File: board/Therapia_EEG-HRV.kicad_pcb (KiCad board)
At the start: 4 copper layers, 61.8 x 45 mm, 141 parts, among them J1 USB-C_16P, J2 Header_2x6

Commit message: R29: the 2026-08-29 functional review, applied as BOM-only changes
An independent review found no blocker. Four of its findings can be fixed
without touching a single track, so they are in; the rest are recorded as
Rev.A-accepted, firmware-mandatory, or Rev.B.

  C_CM1P..C_CM8N (16)  C1588  -> C163508   1nF 50V C0G 0603, was X7R
  C_NLDO_OUT           C12530 -> C23733    4.7uF 10V 0402, was 2.2uF 6.3V
  C_LM_IN              C52923 -> C23733    same part, was 1uF 25V
  C_AVDD_P59           C1525  -> C52923    1uF 0402, was 100nF
  C_VCAP1                     kept, with the reason written down

The C0G swap is the one that matters: those sixteen sit on the electrode
input nodes, and X7R is piezoelectric -- in a wearable that is microphonic
noise straight into the ADC -- while its +-10% spread mismatches each
differential pair and caps the 50 Hz CMRR (SBAS499 12.1). JLC has no Basic
C0G in 0603 at all (base-filtered search returns zero), so this adds one
Extended row, 13 -> 14, about $3.07.

The two electrolytic-substitute cases are settled by Samsung's own curves at
25 C rather than by estimate: C12530 holds 0.543 at 2.5 V = 1.19 uF, under
the 2.2 uF TPS72325 asks for (SLVS346 8.2.1.1); C52923 holds 0.420 at 5 V =
0.42 uF against LM2664's 3.3 uF test circuit (SNVS005). C23733's own curve
was not obtained -- flagged in the fixes file and the report. C_VCAP1 stays:
at AVSS+1.1..1.5 V it comes out at 60-65 uF, short of TI's 100 uF but only
in the direction of a shorter start-up wait.

The board diff is 57 property lines on 19 footprints. All 66,242 other lines
of the .kicad_pcb are unchanged, the CPL and the IPC-D-356 are byte-identical,
and all 14 Gerber/drill/job files match the previous export once each file's
one or two generation-date lines are removed. Fields do not plot; this
measures that rather than asserting it. assembly_top.pdf does change -- it
prints Value from F.Fab -- and the 3D previews differ by 0.03% of pixels,
max channel delta 7/255, which is the rayt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
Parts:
- C_AVDD_P59: value 100nF -> 1uF
- C_CM1N, C_CM1P, C_CM2N, C_CM2P, C_CM3N, C_CM3P, C_CM4N, C_CM4P, C_CM5N, C_CM5P, C_CM6N, C_CM6P, C_CM7N, C_CM7P, C_CM8N, C_CM8P: value 1nF -> 1nF 50V C0G 0603
- C_LM_IN: value 1uF -> 4.7uF 10V X5R 0402
- C_NLDO_OUT: value 2.2uF -> 4.7uF 10V X5R 0402
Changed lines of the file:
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@@
 			)
 		)
-		(property "Value" "1nF"
+		(property "Value" "1nF 50V C0G 0603"
 			(at 0 0 0)
 			(layer "F.Fab")
@@
 			)
 		)
-		(property "MPN" "CL10B102KB8NNNC"
+		(property "MPN" "CL10C102JB8NNNC"
 			(at 0 0 0)
 			(layer "Cmts.User")
@@
 			)
 		)
-		(property "LCSC" "C1588"
+		(property "LCSC" "C163508"
 			(at 0 0 0)
 			(layer "Cmts.User")
@@
 			)
 		)
-		(property "Value" "1nF"
+		(property "Value" "1nF 50V C0G 0603"
 			(at 0 0 0)
 			(layer "F.Fab")
@@
 			)
 		)
-		(property "MPN" "CL10B102KB8NNNC"
+		(property "MPN" "CL10C102JB8NNNC"
 			(at 0 0 0)
 			(layer "Cmts.User")
@@
 			)
 		)
-		(property "LCSC" "C1588"
+		(property "LCSC" "C163508"
 			(at 0 0 0)
 			(layer "Cmts.User")
@@
 			)
 		)
-		(property "Value" "1nF"
+		(property "Value" "1nF 50V C0G 0603"
 			(at 0 0 0)
 			(layer "F.Fab")
@@
 			)
 		)
-		(property "MPN" "CL10B102KB8NNNC"
+		(property "MPN" "CL10C102JB8NNNC"
 			(at 0 0 0)
 			(layer "Cmts.User")
@@
 			)
 		)
-		(property "LCSC" "C1588"
+		(property "LCSC" "C163508"
 			(at 0 0 0)
 			(layer "Cmts.User")
@@
 			)
 		)
-		(property "Value" "1nF"
+		(property "Value" "1nF 50V C0G 0603"
 			(at 0 0 0)
 			(layer "F.Fab")
@@
 			)
 		)
-		(property "MPN" "CL10B102KB8NNNC"
+		(property "MPN" "CL10C102JB8NNNC"
 			(at 0 0 0)
 			(layer "Cmts.User")
@@
 			)
 		)
-		(property "LCSC" "C1588"
+		(property "LCSC" "C163508"
 			(at 0 0 0)
 			(layer "Cmts.User")
@@
 			)
 		)
-		(property "Value" "100nF"
+		(property "Value" "1uF"
 			(at 0 0 90)
 			(layer "F.Fab")
@@
 			)
 		)
-		(property "MPN" "CL05B104KO5NNNC"
+		(property "MPN" "CL05A105KA5NQNC"
 			(at 0 0 0)
 			(layer "Cmts.User")
@@
 			)
 		)
-		(property "LCSC" "C1525"
+		(property "LCSC" "C52923"
 			(at 0 0 0)
 			(layer "Cmts.User")
@@
 			)
 		)
-		(property "Value" "1nF"
+		(property "Value" "1nF 50V C0G 0603"
 			(at 0 0 0)
 			(layer "F.Fab")
@@
 			)
 		)
-		(property "MPN" "CL10B102KB8NNNC"
+		(property "MPN" "CL10C102JB8NNNC"
 			(at 0 0 0)
 			(layer "Cmts.User")
@@
 			)
 		)
-		(property "LCSC" "C1588"
+		(property "LCSC" "C163508"
 			(at 0 0 0)
 			(layer "Cmts.User")
@@
 			)
 		)
-		(property "Value" "1nF"
+		(property "Value" "1nF 50V C0G 0603"
 			(at 0 0 0)
 			(layer "F.Fab")
@@
 			)
 		)
-		(property "MPN" "CL10B102KB8NNNC"
+		(property "MPN" "CL10C102JB8NNNC"
 			(at 0 0 0)
 			(layer "Cmts.User")
@@
 			)
 		)
-		(property "LCSC" "C1588"
+		(property "LCSC" "C163508"
 			(at 0 0 0)
 			(layer "Cmts.User")
@@
 			)
 		)
-		(property "Value" "1nF"
+		(property "Value" "1nF 50V C0G 0603"
 			(at 0 0 0)
 			(layer "F.Fab")
@@
 			)
 		)
-		(property "MPN" "CL10B102KB8NNNC"
+		(property "MPN" "CL10C102JB8NNNC"
 			(at 0 0 0)
 			(layer "Cmts.User")
@@
 			)
 		)
-		(property "LCSC" "C1588"
+		(property "LCSC" "C163508"
 			(at 0 0 0)
 			(layer "Cmts.User")
@@
 			)
 		)
-		(property "Value" "1nF"
+		(property "Value" "1nF 50V C0G 0603"
 			(at 0 0 0)
 			(layer "F.Fab")
@@
 			)
 		)
-		(property "MPN" "CL10B102KB8NNNC"
+		(property "MPN" "CL10C102JB8NNNC"
 			(at 0 0 0)
 			(layer "Cmts.User")
@@
 			)
 		)
-		(property "LCSC" "C1588"
+		(property "LCSC" "C163508"
 			(at 0 0 0)
 			(layer "Cmts.User")
@@
 			)
 		)
-		(property "Value" "1nF"
+		(property "Value" "1nF 50V C0G 0603"
 			(at 0 0 0)
 			(layer "F.Fab")
@@
 			)
 		)
-		(property "MPN" "CL10B102KB8NNNC"
+		(property "MPN" "CL10C102JB8NNNC"
 			(at 0 0 0)
 			(layer "Cmts.User")
@@
 			)
 		)
-		(property "LCSC" "C1588"
+		(property "LCSC" "C163508"
 			(at 0 0 0)
 			(layer "Cmts.User")
@@
 			)
 		)
-		(property "Value" "1nF"
+		(property "Value" "1nF 50V C0G 0603"
 			(at 0 0 0)
 			(layer "F.Fab")
@@
 			)
 		)
-		(property "MPN" "CL10B102KB8NNNC"
+		(property "MPN" "CL10C102JB8NNNC"
 			(at 0 0 0)
 			(layer "Cmts.User")
@@
 			)
 		)
-		(property "LCSC" "C1588"
+		(property "LCSC" "C163508"
 			(at 0 0 0)
 			(layer "Cmts.User")
@@
 			)
 		)
-		(property "Value" "2.2uF"
+		(property "Value" "4.7uF 10V X5R 0402"
 			(at 0 0 90)
 			(layer "F.Fab")
@@
 			)
 		)
-		(property "MPN" "CL05A225MQ5NSNC"
+		(property "MPN" "CL05A475MP5NRNC"
 			(at 0 0 0)
 			(layer "Cmts.User")
@@
 			)
 		)
-		(property "LCSC" "C12530"
+		(property "LCSC" "C23733"
 			(at 0 0 0)
 			(layer "Cmts.User")
@@
 			)
 		)
-		(property "Value" "1nF"
+		(property "Value" "1nF 50V C0G 0603"
 			(at 0 0 0)
 			(layer "F.Fab")
@@
 			)
 		)
-		(property "MPN" "CL10B102KB8NNNC"
+		(property "MPN" "CL10C102JB8NNNC"
 			(at 0 0 0)
 			(layer "Cmts.User")
@@
 			)
 		)
-		(property "LCSC" "C1588"
+		(property "LCSC" "C163508"
 			(at 0 0 0)
 			(layer "Cmts.User")
@@
 			)
 		)
-		(property "Value" "1uF"
+		(property "Value" "4.7uF 10V X5R 0402"
 			(at 0 0 0)
 			(layer "F.Fab")
@@
 			)
 		)
-		(property "MPN" "CL05A105KA5NQNC"
+		(property "MPN" "CL05A475MP5NRNC"
 			(at 0 0 0)
 			(layer "Cmts.User")
@@
 			)
 		)
-		(property "LCSC" "C52923"
+		(property "LCSC" "C23733"
 			(at 0 0 0)
 			(layer "Cmts.User")
@@
 			)
 		)
-		(property "Value" "1nF"
+		(property "Value" "1nF 50V C0G 0603"
 			(at 0 0 0)
 			(layer "F.Fab")
@@
 			)
 		)
-		(property "MPN" "CL10B102KB8NNNC"
+		(property "MPN" "CL10C102JB8NNNC"
 			(at 0 0 0)
 			(layer "Cmts.User")
@@
 			)
 		)
-		(property "LCSC" "C1588"
+		(property "LCSC" "C163508"
 			(at 0 0 0)
 			(layer "Cmts.User")
@@
 			)
 		)
-		(property "Value" "1nF"
+		(property "Value" "1nF 50V C0G 0603"
 			(at 0 0 0)
 			(layer "F.Fab")
@@
 			)
 		)
-		(property "MPN" "CL10B102KB8NNNC"
+		(property "MPN" "CL10C102JB8NNNC"
 			(at 0 0 0)
 			(layer "Cmts.User")
@@
 			)
 		)
-		(property "LCSC" "C1588"
+		(property "LCSC" "C163508"
 			(at 0 0 0)
 			(layer "Cmts.User")
@@
 			)
 		)
-		(property "Value" "1nF"
+		(property "Value" "1nF 50V C0G 0603"
 			(at 0 0 0)
 			(layer "F.Fab")
@@
 			)
 		)
-		(property "MPN" "CL10B102KB8NNNC"
+		(property "MPN" "CL10C102JB8NNNC"
 			(at 0 0 0)
 			(layer "Cmts.User")
@@
 			)
 		)
-		(property "LCSC" "C1588"
+		(property "LCSC" "C163508"
 			(at 0 0 0)
 			(layer "Cmts.User")
@@
 			)
 		)
-		(property "Value" "1nF"
+		(property "Value" "1nF 50V C0G 0603"
 			(at 0 0 0)
 			(layer "F.Fab")
@@
 			)
 		)
-		(property "MPN" "CL10B102KB8NNNC"
+		(property "MPN" "CL10C102JB8NNNC"
 			(at 0 0 0)
 			(layer "Cmts.User")
@@
 			)
 		)
-		(property "LCSC" "C1588"
+		(property "LCSC" "C163508"
 			(at 0 0 0)
 			(layer "Cmts.User")
@@
 			)
 		)
-		(property "Value" "1nF"
+		(property "Value" "1nF 50V C0G 0603"
 			(at 0 0 0)
 			(layer "F.Fab")
@@
 			)
 		)
-		(property "MPN" "CL10B102KB8NNNC"
+		(property "MPN" "CL10C102JB8NNNC"
 			(at 0 0 0)
 			(layer "Cmts.User")
@@
 			)
 		)
-		(property "LCSC" "C1588"
+		(property "LCSC" "C163508"
 			(at 0 0 0)
 			(layer "Cmts.User")

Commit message: R29-6: the two auto-reset base resistors become 470k, on simulation evidence
The ngspice case sim/cases/esp32_autoreset.py found ESP_EN idling at 4.238 V
and ESP_IO0 at 4.203 V against the ESP32's 3.6 V absolute maximum. The CH340C
runs from USB_5V, so DTR#/RTS# idle at 5 V; both handshake lines high leaves
each transistor off with its base above its 3.3 V collector, forward-biasing
the base-collector junction into the 10 k pull-ups.

The first proposal was 100 k, reasoning that ten times the resistance is a
tenth of the current. The simulation rejected it. The off-side device is in
reverse-active mode, so the collector pushes (1 + BR) times the base current
into the node -- 7.63 uA of base current against 38.71 uA of injection, a
ratio of 5.07 against the model's BR = 4 -- and the loop self-limits, because
raising R lowers the node and so raises the drop across R. 10 k -> 100 k cut
the current only 2.4x (93.85 -> 38.71 uA) and left ESP_EN at 3.687 V, still
over the limit.

470 k (C23178, UNI-ROYAL 0603WAF4703T5E, JLC Basic, stock 1,256,032) gives
ESP_EN 3.414 V, ESP_IO0 3.398 V, injection 11.40 uA. It was picked over 330 k
and 1 M by sweeping the S8050's reverse beta over BR = 1..10, which the
datasheet does not publish: 100 k passes only for BR <= 2, 150 k and 220 k
fail at BR >= 7, 330 k passes with 8 mV of margin, 470 k holds 3.347..3.523 V
for 77 mV in the worst corner while keeping more base drive than 1 M.

The esptool truth table is unchanged (ON 0.066 / 0.072 V, OFF 3.297 / 3.300 V)
and the ON-state base current of 9.33 uA gives 1.87 mA of collector capability
at the hFE 200 bin, against a 0.33 mA pull-up; C_EN_DLY discharges in ~1.6 ms
against esptool's 100 ms reset pulse.

Also replaces the EN-delay criterion. It demanded "EN rises >= 10 ms after the
3.3 V rail", a threshold no datasheet states; Espressif requires only that EN
stay low until the supply is stable and recommends the 10 k / 1 uF RC as the
means. Against the invented number the derated capaci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
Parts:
- R_Q_EN_B, R_Q_IO0_B: value 10k -> 470k
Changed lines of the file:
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@@
 			)
 		)
-		(property "Value" "10k"
+		(property "Value" "470k"
 			(at 0 0 90)
 			(layer "F.Fab")
@@
 			)
 		)
-		(property "MPN" "0603WAF1002T5E"
+		(property "MPN" "0603WAF4703T5E"
 			(at 0 0 0)
 			(layer "Cmts.User")
@@
 			)
 		)
-		(property "LCSC" "C25804"
+		(property "LCSC" "C23178"
 			(at 0 0 0)
 			(layer "Cmts.User")
@@
 			)
 		)
-		(property "Value" "10k"
+		(property "Value" "470k"
 			(at 0 0 90)
 			(layer "F.Fab")
@@
 			)
 		)
-		(property "MPN" "0603WAF1002T5E"
+		(property "MPN" "0603WAF4703T5E"
 			(at 0 0 0)
 			(layer "Cmts.User")
@@
 			)
 		)
-		(property "LCSC" "C25804"
+		(property "LCSC" "C23178"
 			(at 0 0 0)
 			(layer "Cmts.User")

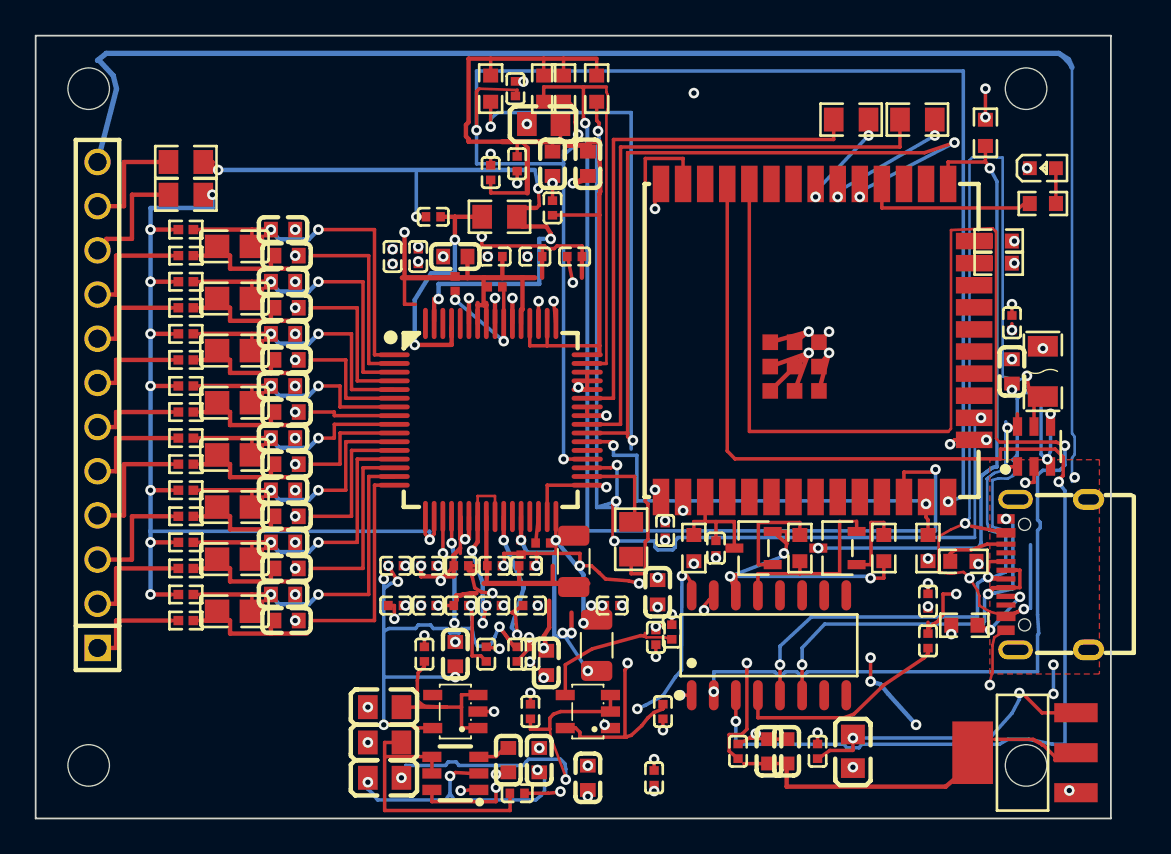
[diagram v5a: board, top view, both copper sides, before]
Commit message: S7v: move 114 vias out of the SMD pads they sat in; ACCEPTANCE I; fab Y9
Y8 had 106 via drills inside SMD solder-mask openings on a Tented 4-layer
order. scripts/66_fix_via_in_pad.py dogbones each out of its pad (two dead
AVSS vias removed, two neighbouring UART tracks moved to make room), and
scripts/67_viapad_gate.py (ACCEPTANCE I) checks the package with its own
Gerber reader and the harness S7_viapad: 0 and pass. DRC 0/0, parity 0,
IN1P-IN8N path length unchanged, BOM/CPL unchanged. Y8 must not be paid.

Co-Authored-By: Claude Opus 5.5 (1M context) <noreply@anthropic.com>
Claude-Session: https://claude.ai/code/session_01BbaSxDrhhKaR1T3EhiM8tM
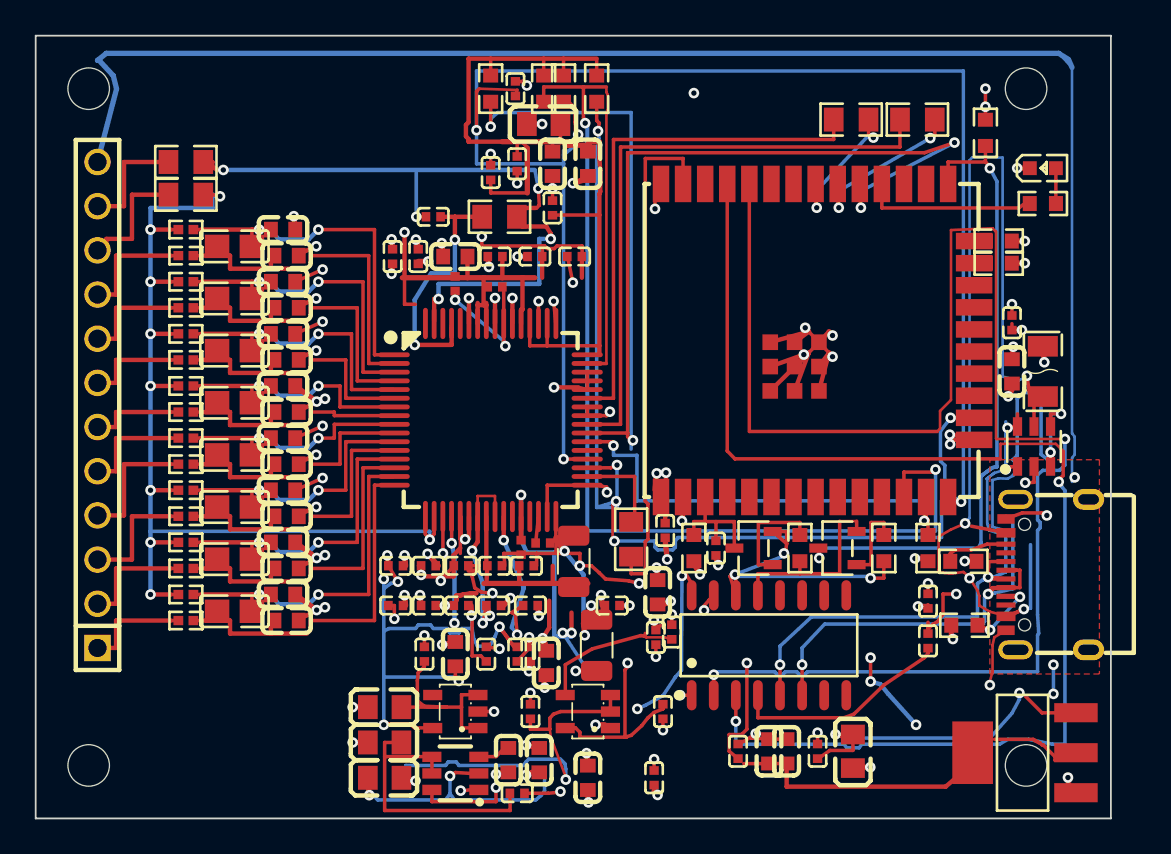
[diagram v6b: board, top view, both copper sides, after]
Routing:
- net GND: track 84.1 -> 134.1 mm
- net VCAP1: track 14.5 -> 21.1 mm
- net AVDD: track 54.1 -> 60.0 mm
- net USB_5V: track 14.6 -> 20.4 mm
- net AVSS: track 87.1 -> 92.2 mm, vias 21 -> 19
- net VDD_ESP: track 36.5 -> 40.6 mm
- net VNEG5: track 15.5 -> 18.5 mm
- net V_3V3_IN: track 17.0 -> 19.1 mm
- net USB_DM: track 43.7 -> 45.7 mm
- net ADS_START: track 24.7 -> 26.6 mm
- net SPI_MISO: track 7.16 -> 9.01 mm
- net V_NLDO_IN: track 21.0 -> 22.6 mm
- net ADS_RESET_N: track 91.2 -> 92.7 mm
- net SPI_SCK: track 9.18 -> 10.4 mm
- net ADS_CS_N: track 75.2 -> 76.4 mm
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
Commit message: Y9 re-export: S7v+S7p+S7d wired into run.sh, rulings recorded, all gates green
run.sh gains S7p, S7d and S7_paste; S7b attributes S7d's removals; via counts
239 -> 234 (IPC-D-356 / ODB++ constants). ACCEPTANCE: lead rulings on SRB1
(<= 1.0 mm), VCAP1 (pin-side unchanged, loop areas unchanged) and CM GND vias
in addendum 3; criteria J and K in addendum 4. Board and fab regenerated from
the pre-S7v board: DRC 0/0, dangling 0, via-in-pad 0, paste past pad 0.

Co-Authored-By: Claude Opus 5.5 (1M context) <noreply@anthropic.com>
Claude-Session: https://claude.ai/code/session_01BbaSxDrhhKaR1T3EhiM8tM
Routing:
- net AVSS: track 92.2 -> 84.3 mm
- net VDD_ESP: track 40.6 -> 35.5 mm, vias 13 -> 9
- net USB_VBUS_RAW: track 58.2 -> 54.5 mm, vias 4 -> 3
- net GND: track 134.1 -> 131.3 mm
- net VCAP1: track 21.1 -> 20.0 mm
- net VREFP: track 11.9 -> 10.7 mm
- net USB_DP: track 34.0 -> 33.3 mm
